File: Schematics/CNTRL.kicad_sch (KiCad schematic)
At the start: 46 parts, among them SW1 RotaryEncoder_Switch, SW2 RotaryEncoder_Switch, SW3 RotaryEncoder_Switch, SW4 RotaryEncoder_Switch, U6 PCA9555PW

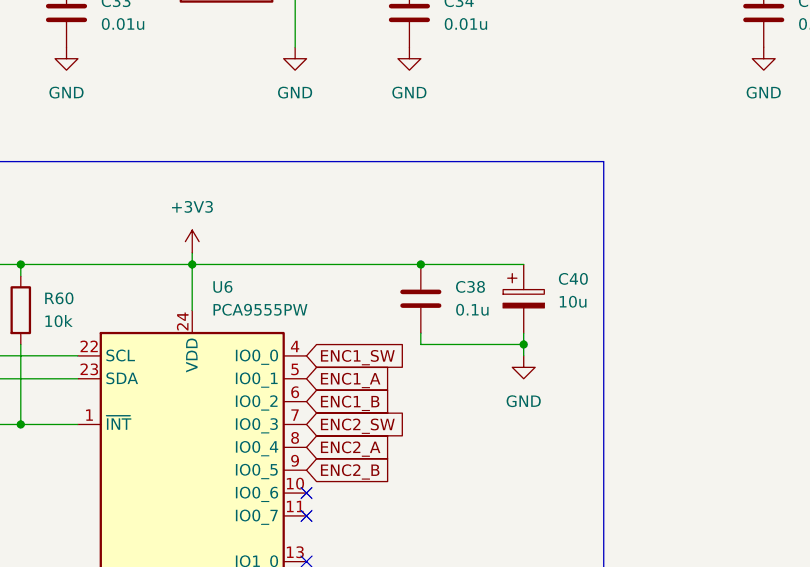
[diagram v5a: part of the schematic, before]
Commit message: Added all footprints, updated PCB
Added footprints using uni available components where possible. Might be necessary to change op-amps as they are large and not made for audio. PCB has a mockup of component placements but probably needs expanded.
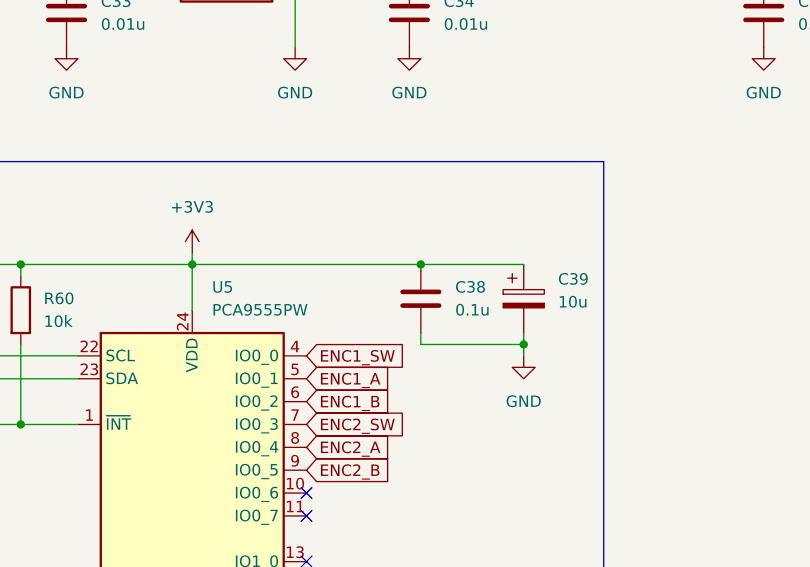
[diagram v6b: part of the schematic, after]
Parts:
- C26, C27, C28, C29, C30, C31, C32, C33, C34, C35, C36, C37, C38: footprint (none) -> Capacitor_SMD:C_0805_2012Metric_Pad1.18x1.45mm_HandSolder
- R34, R35, R36, R37, R38, R39, R40, R41, R42, R43, R44, R45, R46, R47, R48, R49, R50, R51, R52, R53, R54, R55, R56, R57, R58, R59, R60: footprint Resistor_SMD:R_0603_1608Metric_Pad0.98x0.95mm_HandSolder -> Resistor_SMD:R_0805_2012Metric_Pad1.20x1.40mm_HandSolder
- renumbered C40 to C39, U6 to U5
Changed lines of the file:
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@@
 			)
 		)
-		(property "Footprint" "Resistor_SMD:R_0603_1608Metric_Pad0.98x0.95mm_HandSolder"
+		(property "Footprint" "Resistor_SMD:R_0805_2012Metric_Pad1.20x1.40mm_HandSolder"
 			(at 202.438 87.63 90)
 			(effects
@@
 			)
 		)
-		(property "Footprint" "Resistor_SMD:R_0603_1608Metric_Pad0.98x0.95mm_HandSolder"
+		(property "Footprint" "Resistor_SMD:R_0805_2012Metric_Pad1.20x1.40mm_HandSolder"
 			(at 194.31 98.298 90)
 			(effects
@@
 			)
 		)
-		(property "Footprint" "Resistor_SMD:R_0603_1608Metric_Pad0.98x0.95mm_HandSolder"
+		(property "Footprint" "Resistor_SMD:R_0805_2012Metric_Pad1.20x1.40mm_HandSolder"
 			(at 87.63 56.388 90)
 			(effects
@@
 			)
 		)
-		(property "Footprint" ""
+		(property "Footprint" "Capacitor_SMD:C_0805_2012Metric_Pad1.18x1.45mm_HandSolder"
 			(at 201.6252 67.31 0)
 			(effects
@@
 			)
 		)
-		(property "Footprint" "Resistor_SMD:R_0603_1608Metric_Pad0.98x0.95mm_HandSolder"
+		(property "Footprint" "Resistor_SMD:R_0805_2012Metric_Pad1.20x1.40mm_HandSolder"
 			(at 28.448 87.63 90)
 			(effects
@@
 			)
 		)
-		(property "Footprint" "Resistor_SMD:R_0603_1608Metric_Pad0.98x0.95mm_HandSolder"
+		(property "Footprint" "Resistor_SMD:R_0805_2012Metric_Pad1.20x1.40mm_HandSolder"
 			(at 148.59 98.298 90)
 			(effects
@@
 			)
 		)
-		(property "Footprint" "Resistor_SMD:R_0603_1608Metric_Pad0.98x0.95mm_HandSolder"
+		(property "Footprint" "Resistor_SMD:R_0805_2012Metric_Pad1.20x1.40mm_HandSolder"
 			(at 164.338 45.72 90)
 			(effects
@@
 			)
 		)
-		(property "Footprint" "Resistor_SMD:R_0603_1608Metric_Pad0.98x0.95mm_HandSolder"
+		(property "Footprint" "Resistor_SMD:R_0805_2012Metric_Pad1.20x1.40mm_HandSolder"
 			(at 41.91 56.388 90)
 			(effects
@@
 			)
 		)
-		(property "Footprint" "Resistor_SMD:R_0603_1608Metric_Pad0.98x0.95mm_HandSolder"
+		(property "Footprint" "Resistor_SMD:R_0805_2012Metric_Pad1.20x1.40mm_HandSolder"
 			(at 194.31 56.388 90)
 			(effects
@@
 			)
 		)
-		(property "Footprint" "Resistor_SMD:R_0603_1608Metric_Pad0.98x0.95mm_HandSolder"
+		(property "Footprint" "Resistor_SMD:R_0805_2012Metric_Pad1.20x1.40mm_HandSolder"
 			(at 41.91 98.298 90)
 			(effects
@@
 			)
 		)
-		(property "Footprint" ""
+		(property "Footprint" "Capacitor_SMD:C_0805_2012Metric_Pad1.18x1.45mm_HandSolder"
 			(at 163.5252 67.31 0)
 			(effects
@@
 			)
 		)
-		(property "Footprint" ""
+		(property "Footprint" "Capacitor_SMD:C_0805_2012Metric_Pad1.18x1.45mm_HandSolder"
 			(at 56.8452 109.22 0)
 			(effects
@@
 			)
 		)
-		(property "Footprint" "Resistor_SMD:R_0603_1608Metric_Pad0.98x0.95mm_HandSolder"
+		(property "Footprint" "Resistor_SMD:R_0805_2012Metric_Pad1.20x1.40mm_HandSolder"
 			(at 148.59 56.388 90)
 			(effects
@@
 			)
 		)
-		(property "Footprint" "Resistor_SMD:R_0603_1608Metric_Pad0.98x0.95mm_HandSolder"
+		(property "Footprint" "Resistor_SMD:R_0805_2012Metric_Pad1.20x1.40mm_HandSolder"
 			(at 167.64 103.378 90)
 			(effects
@@
 		(dnp no)
 		(fields_autoplaced yes)
-		(property "Reference" "C40"
+		(property "Reference" "C39"
 			(at 110.49 135.0009 0)
 			(effects
@@
 			(project "Harmoniser HAT"
 				(path "/41751dd2-97f9-4cc6-b9e6-b561e5949053/5d678f4e-03b5-43f5-b100-a64e850a5e5c"
-					(reference "C40")
+					(reference "C39")
 					(unit 1)
 				)
@@
 			)
 		)
-		(property "Footprint" ""
+		(property "Footprint" "Capacitor_SMD:C_0805_2012Metric_Pad1.18x1.45mm_HandSolder"
 			(at 201.6252 109.22 0)
 			(effects
@@
 			)
 		)
-		(property "Footprint" ""
+		(property "Footprint" "Capacitor_SMD:C_0805_2012Metric_Pad1.18x1.45mm_HandSolder"
 			(at 94.9452 67.31 0)
 			(effects
@@
 			)
 		)
-		(property "Footprint" "Resistor_SMD:R_0603_1608Metric_Pad0.98x0.95mm_HandSolder"
+		(property "Footprint" "Resistor_SMD:R_0805_2012Metric_Pad1.20x1.40mm_HandSolder"
 			(at 164.338 87.63 90)
 			(effects
@@
 			)
 		)
-		(property "Footprint" "Resistor_SMD:R_0603_1608Metric_Pad0.98x0.95mm_HandSolder"
+		(property "Footprint" "Resistor_SMD:R_0805_2012Metric_Pad1.20x1.40mm_HandSolder"
 			(at 60.96 61.468 90)
 			(effects
@@
 			)
 		)
-		(property "Footprint" ""
+		(property "Footprint" "Capacitor_SMD:C_0805_2012Metric_Pad1.18x1.45mm_HandSolder"
 			(at 56.8452 67.31 0)
 			(effects
@@
 			)
 		)
-		(property "Footprint" "Resistor_SMD:R_0603_1608Metric_Pad0.98x0.95mm_HandSolder"
+		(property "Footprint" "Resistor_SMD:R_0805_2012Metric_Pad1.20x1.40mm_HandSolder"
 			(at 57.658 45.72 90)
 			(effects
@@
 			)
 		)
-		(property "Footprint" ""
+		(property "Footprint" "Capacitor_SMD:C_0805_2012Metric_Pad1.18x1.45mm_HandSolder"
 			(at 27.6352 109.22 0)
 			(effects
@@
 			)
 		)
-		(property "Footprint" "Resistor_SMD:R_0603_1608Metric_Pad0.98x0.95mm_HandSolder"
+		(property "Footprint" "Resistor_SMD:R_0805_2012Metric_Pad1.20x1.40mm_HandSolder"
 			(at 28.448 45.72 90)
 			(effects
@@
 			)
 		)
-		(property "Footprint" "Resistor_SMD:R_0603_1608Metric_Pad0.98x0.95mm_HandSolder"
+		(property "Footprint" "Resistor_SMD:R_0805_2012Metric_Pad1.20x1.40mm_HandSolder"
 			(at 31.242 138.43 90)
 			(effects
@@
 			)
 		)
-		(property "Footprint" "Resistor_SMD:R_0603_1608Metric_Pad0.98x0.95mm_HandSolder"
+		(property "Footprint" "Resistor_SMD:R_0805_2012Metric_Pad1.20x1.40mm_HandSolder"
 			(at 60.96 103.378 90)
 			(effects
@@
 			)
 		)
-		(property "Footprint" "Resistor_SMD:R_0603_1608Metric_Pad0.98x0.95mm_HandSolder"
+		(property "Footprint" "Resistor_SMD:R_0805_2012Metric_Pad1.20x1.40mm_HandSolder"
 			(at 167.64 61.468 90)
 			(effects
@@
 			)
 		)
-		(property "Footprint" ""
+		(property "Footprint" "Capacitor_SMD:C_0805_2012Metric_Pad1.18x1.45mm_HandSolder"
 			(at 94.9452 109.22 0)
 			(effects
@@
 			)
 		)
-		(property "Footprint" "Resistor_SMD:R_0603_1608Metric_Pad0.98x0.95mm_HandSolder"
+		(property "Footprint" "Resistor_SMD:R_0805_2012Metric_Pad1.20x1.40mm_HandSolder"
 			(at 202.438 45.72 90)
 			(effects
@@
 			)
 		)
-		(property "Footprint" ""
+		(property "Footprint" "Capacitor_SMD:C_0805_2012Metric_Pad1.18x1.45mm_HandSolder"
 			(at 134.3152 109.22 0)
 			(effects
@@
 			)
 		)
-		(property "Footprint" "Resistor_SMD:R_0603_1608Metric_Pad0.98x0.95mm_HandSolder"
+		(property "Footprint" "Resistor_SMD:R_0805_2012Metric_Pad1.20x1.40mm_HandSolder"
 			(at 49.022 138.43 90)
 			(effects
@@
 			)
 		)
-		(property "Footprint" "Resistor_SMD:R_0603_1608Metric_Pad0.98x0.95mm_HandSolder"
+		(property "Footprint" "Resistor_SMD:R_0805_2012Metric_Pad1.20x1.40mm_HandSolder"
 			(at 87.63 98.298 90)
 			(effects
@@
 			)
 		)
-		(property "Footprint" ""
+		(property "Footprint" "Capacitor_SMD:C_0805_2012Metric_Pad1.18x1.45mm_HandSolder"
 			(at 96.2152 140.97 0)
 			(effects
@@
 			)
 		)
-		(property "Footprint" "Resistor_SMD:R_0603_1608Metric_Pad0.98x0.95mm_HandSolder"
+		(property "Footprint" "Resistor_SMD:R_0805_2012Metric_Pad1.20x1.40mm_HandSolder"
 			(at 57.658 87.63 90)
 			(effects
@@
 			)
 		)
-		(property "Footprint" "Resistor_SMD:R_0603_1608Metric_Pad0.98x0.95mm_HandSolder"
+		(property "Footprint" "Resistor_SMD:R_0805_2012Metric_Pad1.20x1.40mm_HandSolder"
 			(at 135.128 45.72 90)
 			(effects
@@
 			)
 		)
-		(property "Footprint" ""
+		(property "Footprint" "Capacitor_SMD:C_0805_2012Metric_Pad1.18x1.45mm_HandSolder"
 			(at 134.3152 67.31 0)
 			(effects
@@
 			)
 		)
-		(property "Footprint" "Resistor_SMD:R_0603_1608Metric_Pad0.98x0.95mm_HandSolder"
+		(property "Footprint" "Resistor_SMD:R_0805_2012Metric_Pad1.20x1.40mm_HandSolder"
 			(at 40.132 138.43 90)
 			(effects
@@
 			)
 		)
-		(property "Footprint" "Resistor_SMD:R_0603_1608Metric_Pad0.98x0.95mm_HandSolder"
+		(property "Footprint" "Resistor_SMD:R_0805_2012Metric_Pad1.20x1.40mm_HandSolder"
 			(at 95.758 45.72 90)
 			(effects
@@
 		(dnp no)
 		(fields_autoplaced yes)
-		(property "Reference" "U6"
+		(property "Reference" "U5"
 			(at 72.0441 135.89 0)
 			(effects
@@
 			(project ""
 				(path "/41751dd2-97f9-4cc6-b9e6-b561e5949053/5d678f4e-03b5-43f5-b100-a64e850a5e5c"
-					(reference "U6")
+					(reference "U5")
 					(unit 1)
 				)
@@
 			)
 		)
-		(property "Footprint" ""
+		(property "Footprint" "Capacitor_SMD:C_0805_2012Metric_Pad1.18x1.45mm_HandSolder"
 			(at 27.6352 67.31 0)
 			(effects
@@
 			)
 		)
-		(property "Footprint" ""
+		(property "Footprint" "Capacitor_SMD:C_0805_2012Metric_Pad1.18x1.45mm_HandSolder"
 			(at 163.5252 109.22 0)
 			(effects
@@
 			)
 		)
-		(property "Footprint" "Resistor_SMD:R_0603_1608Metric_Pad0.98x0.95mm_HandSolder"
+		(property "Footprint" "Resistor_SMD:R_0805_2012Metric_Pad1.20x1.40mm_HandSolder"
 			(at 135.128 87.63 90)
 			(effects
@@
 			)
 		)
-		(property "Footprint" "Resistor_SMD:R_0603_1608Metric_Pad0.98x0.95mm_HandSolder"
+		(property "Footprint" "Resistor_SMD:R_0805_2012Metric_Pad1.20x1.40mm_HandSolder"
 			(at 95.758 87.63 90)
 			(effects

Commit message: Adjusted Capacitor Footprints
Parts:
- C39: footprint Capacitor_SMD:CP_Elec_5x5.4 -> Capacitor_SMD:CP_Elec_4x5.7
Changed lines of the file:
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@@
 			)
 		)
-		(property "Footprint" "Capacitor_SMD:CP_Elec_5x5.4"
+		(property "Footprint" "Capacitor_SMD:CP_Elec_4x5.7"
 			(at 107.6452 140.97 0)
 			(effects

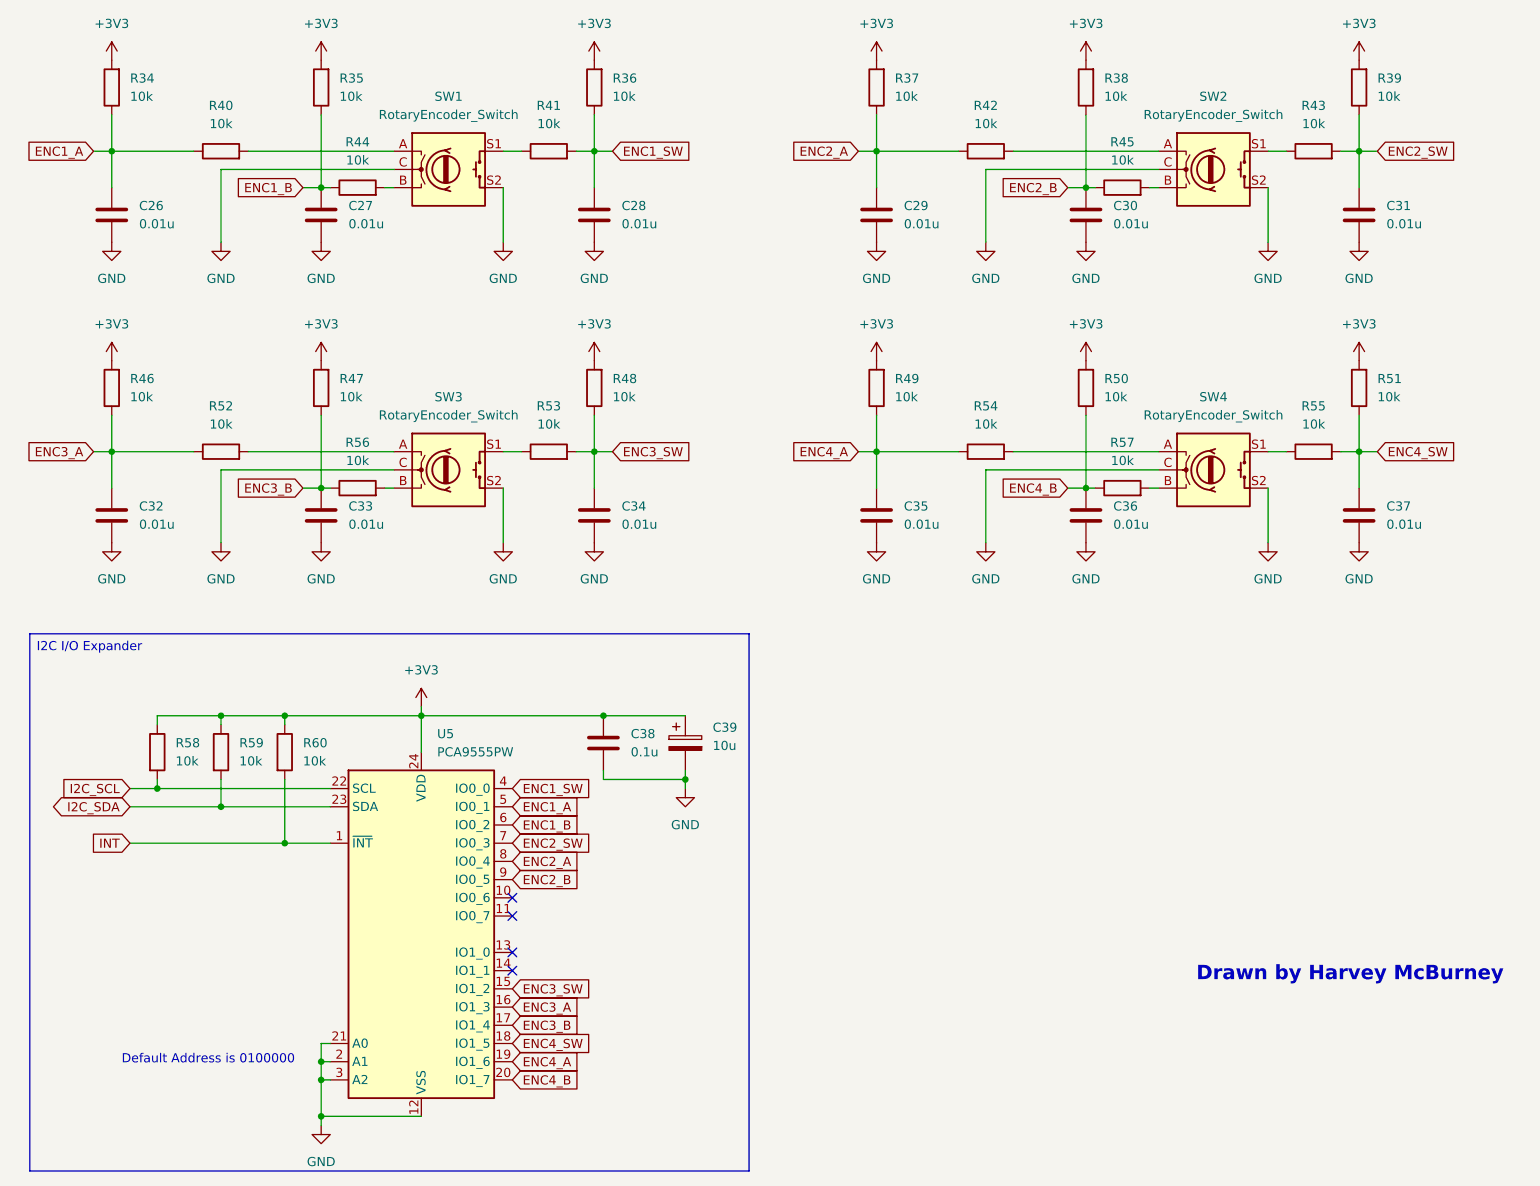
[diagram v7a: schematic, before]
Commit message: Changed footprints, added 3d model to GPIO
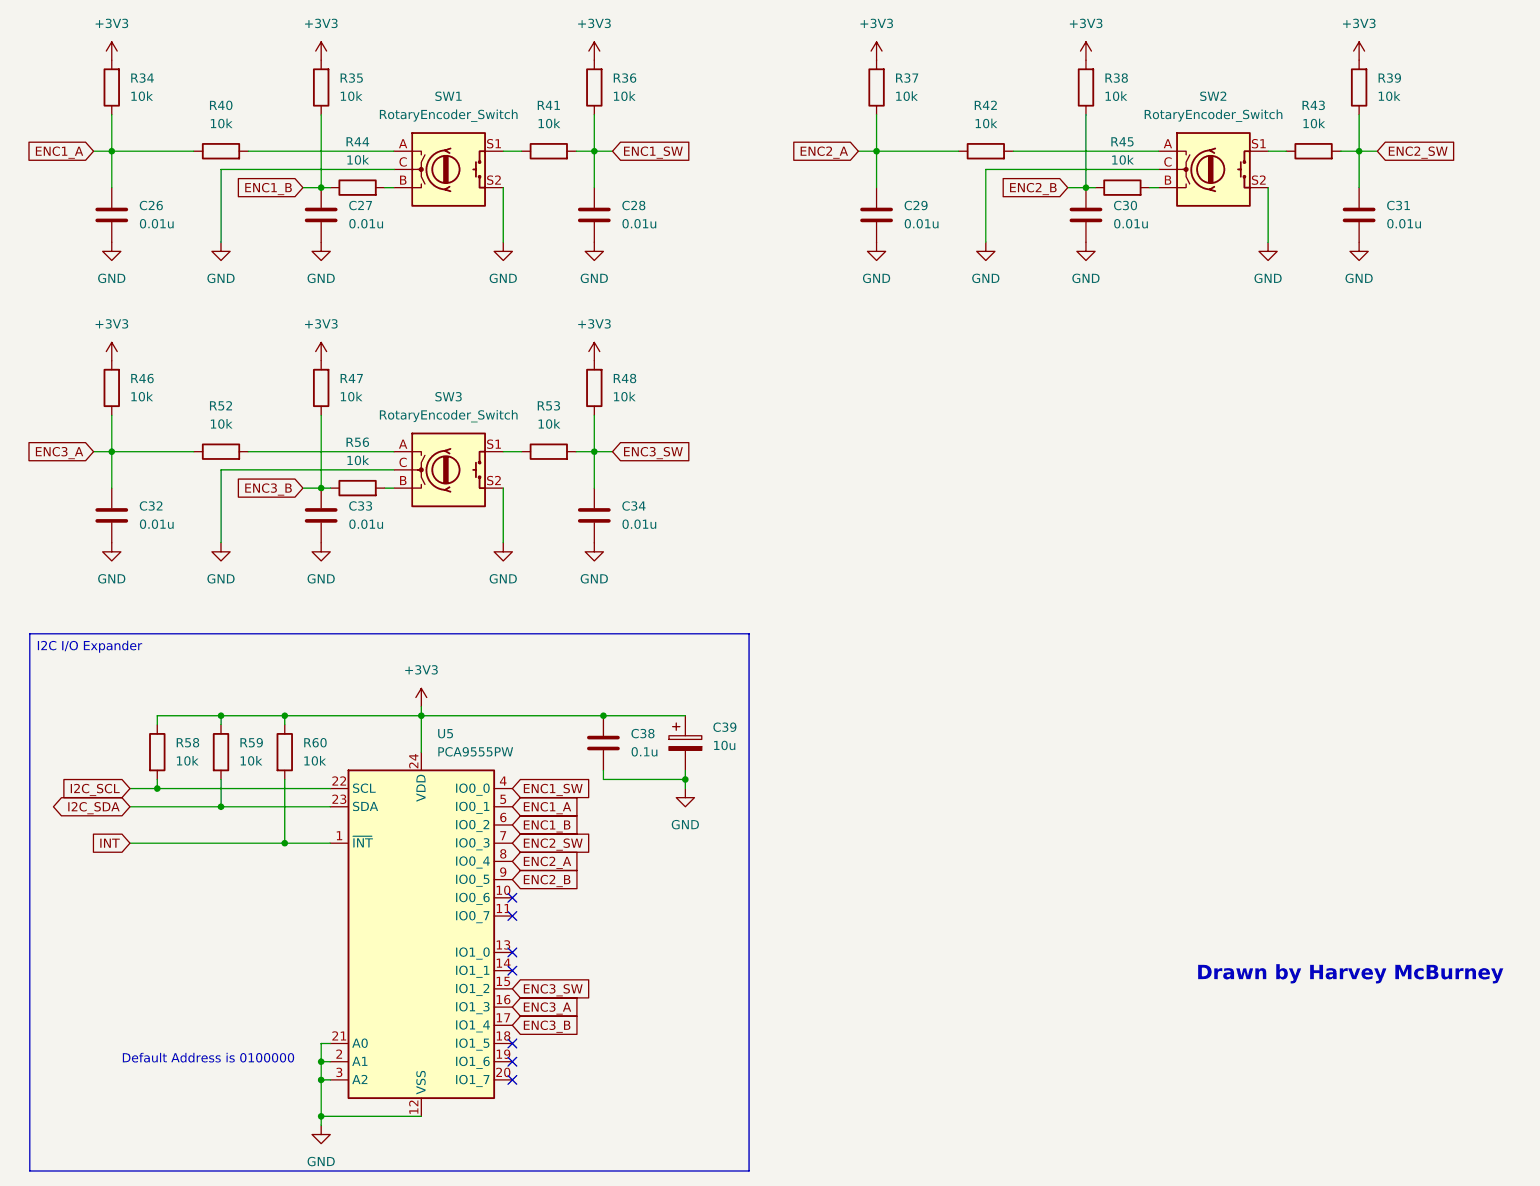
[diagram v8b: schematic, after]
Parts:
- removed C35, C36, C37: 0.01u, Capacitor_SMD:C_0805_2012Metric_Pad1.18x1.45mm_HandSolder, symbol Device:C
- removed R49, R50, R51, R54, R55, R57: 10k, Resistor_SMD:R_0805_2012Metric_Pad1.20x1.40mm_HandSolder, symbol Device:R
- removed SW4: RotaryEncoder_Switch, Rotary_Encoder:RotaryEncoder_Bourns_Vertical_PEC12R-3x17F-Sxxxx, symbol Device:RotaryEncoder_Switch
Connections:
- net ENC4_A: no longer names the net of U5.19 (IO1_6)
- net ENC4_B: no longer names the net of U5.20 (IO1_7)
- net ENC4_SW: no longer names the net of U5.18 (IO1_5)
- no-connect marks 4 -> 7
